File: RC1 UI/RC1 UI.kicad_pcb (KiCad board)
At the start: 2 copper layers, 99.1 x 99.1 mm, 45 parts, among them J1 KB, J2 RC1_UI_Port, M1 Mounting, M2 Mounting, M3 Mounting, M4 Mounting, Q1 2N3906, Q2 2N3906, Q3 2N3906, Q4 2N3906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

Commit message: Added serial to UI schematic
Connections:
- net /ROW_1 renamed /ROW1
- J1 pad 1: /2A6 -> /PA6
- J1 pad 10: /ROW_0 -> /ROW2
- J1 pad 12: (no net) -> /KP_ST
- J1 pad 13: (no net) -> /KP_RS
- J1 pad 15: (no net) -> SST_OUT
- J1 pad 2: /2A5 -> /PA5
- J1 pad 3: /2A4 -> /PA4
- J1 pad 4: /2A3 -> /PA3
- J1 pad 5: /2A2 -> /PA2
- J1 pad 6: /2A1 -> /PA1
- J1 pad 7: /2A0 -> /PA0
- J1 pad 8: /ROW_2 -> /ROW0
- J2 pad 1: (no net) -> GND
- J2 pad 12: (no net) -> /PA0
- J2 pad 13: (no net) -> /PA6
- J2 pad 14: (no net) -> /PA1
- J2 pad 15: (no net) -> /PA5
- J2 pad 16: (no net) -> /PA2
- J2 pad 17: (no net) -> /PA4
- J2 pad 18: (no net) -> /PA3
- J2 pad 2: (no net) -> GND
- J2 pad 3: (no net) -> /PB4
- J2 pad 33: (no net) -> SST_OUT
- J2 pad 34: (no net) -> SYNC
- J2 pad 35: (no net) -> K7
- J2 pad 37: (no net) -> /KP_RS
- J2 pad 38: (no net) -> /KP_ST
- J2 pad 4: (no net) -> /PB3
- J2 pad 6: (no net) -> /PB2
- J2 pad 8: (no net) -> /PB1
- U1 pad 1: /ROW_0 -> /ROW0
- U1 pad 12: (no net) -> /PB4
- U1 pad 13: (no net) -> /PB3
- U1 pad 14: (no net) -> /PB2
- U1 pad 15: (no net) -> /PB1
- U1 pad 3: /ROW_2 -> /ROW2
- U2 pad 1: /2A0 -> /PA0
- U2 pad 11: /2A4 -> /PA4
- U2 pad 13: /2A1 -> /PA0
- U2 pad 3: /2A2 -> /PA2
- U2 pad 5: /2A5 -> /PA5
- U2 pad 9: /2A6 -> /PA6
- U3 pad 1: (no net) -> K7
- U3 pad 2: (no net) -> SYNC
- U3 pad 5: /2A3 -> /PA3

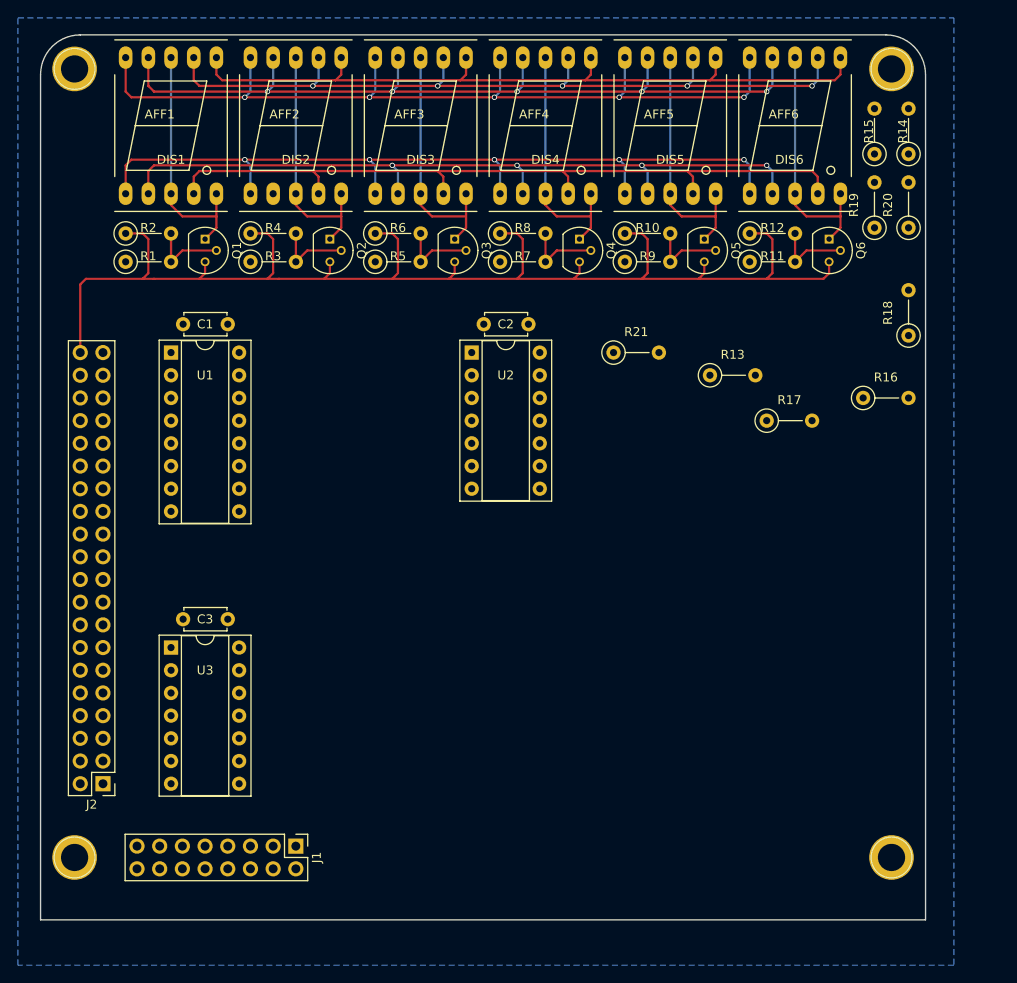
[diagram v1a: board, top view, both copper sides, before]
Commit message: UI layout done
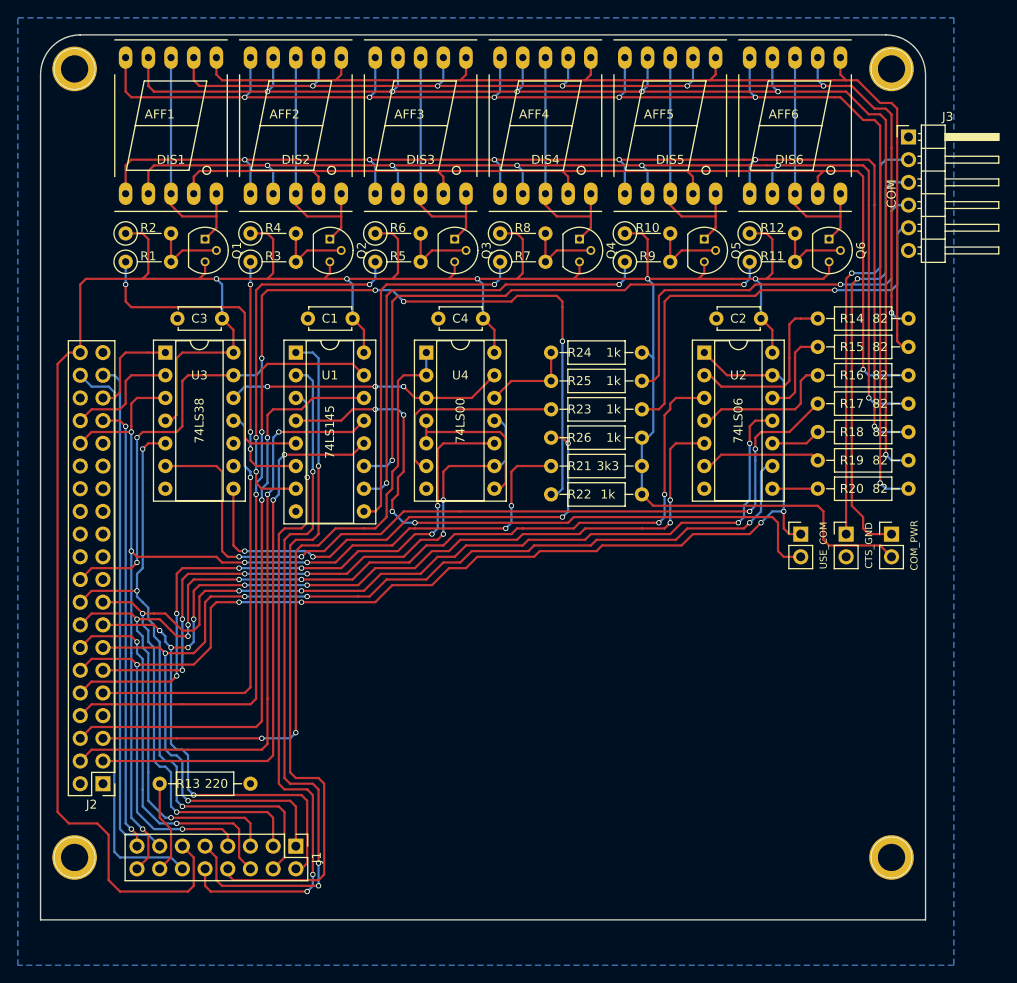
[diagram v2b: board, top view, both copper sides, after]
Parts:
- added C4: 100nF, Capacitors_THT:C_Disc_D4.7mm_W2.5mm_P5.00mm, F.Cu at (157.5, 68.6)
- added J3: COM, Pin_Headers:Pin_Header_Angled_1x06_Pitch2.54mm, F.Cu at (205.1, 48.3)
- added JP1: COM_PWR, Pin_Headers:Pin_Header_Straight_1x02_Pitch2.54mm, F.Cu at (203.2, 92.7)
- added JP2: CTS_GND, Pin_Headers:Pin_Header_Straight_1x02_Pitch2.54mm, F.Cu at (198.1, 92.7)
- added JP3: USE_COM, Pin_Headers:Pin_Header_Straight_1x02_Pitch2.54mm, F.Cu at (193.0, 92.7)
- added R22: 1k, Resistors_THT:R_Axial_DIN0207_L6.3mm_D2.5mm_P10.16mm_Horizontal, F.Cu at (175.3, 88.3)
- added R23: 1k, Resistors_THT:R_Axial_DIN0207_L6.3mm_D2.5mm_P10.16mm_Horizontal, F.Cu at (175.3, 78.7)
- added R24: 1k, Resistors_THT:R_Axial_DIN0207_L6.3mm_D2.5mm_P10.16mm_Horizontal, F.Cu at (175.3, 72.4)
- added R25: 1k, Resistors_THT:R_Axial_DIN0207_L6.3mm_D2.5mm_P10.16mm_Horizontal, F.Cu at (175.3, 75.6)
- added R26: 1k, Resistors_THT:R_Axial_DIN0207_L6.3mm_D2.5mm_P10.16mm_Horizontal, F.Cu at (175.3, 81.9)
- added U4: 74LS00, Housings_DIP:DIP-14_W7.62mm_Socket, F.Cu at (151.1, 72.4)
- R13, R14, R15, R16, R17, R18, R19, R20, R21: footprint Resistors_THT:R_Axial_DIN0207_L6.3mm_D2.5mm_P5.08mm_Vertical -> Resistors_THT:R_Axial_DIN0207_L6.3mm_D2.5mm_P10.16mm_Horizontal
- moved R13 68.8 mm to (131.4, 120.7), turned to 180 degrees
- moved C3 33.7 mm to (128.3, 68.6)
- moved U3 33.0 mm to (121.9, 72.4)
- moved R20 30.9 mm to (194.9, 87.6), turned to 0 degrees
- moved R19 26.8 mm to (194.9, 84.5), turned to 0 degrees
- moved C2 26.0 mm to (188.6, 68.6)
- moved U2 26.0 mm to (182.2, 72.4)
- moved R15 22.5 mm to (194.9, 71.8), turned to 0 degrees
- moved R14 21.0 mm to (194.9, 68.6), turned to 0 degrees
- moved R18 14.8 mm to (194.9, 81.3), turned to 0 degrees
- moved R21 14.5 mm to (165.1, 85.1)
- moved C1 14.0 mm to (142.9, 68.6)
- moved U1 14.0 mm to (136.5, 72.4)
- moved R17 6.02 mm to (194.9, 78.1)
- moved R16 5.68 mm to (194.9, 74.9)
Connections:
- J2 pad 10: (no net) -> /PB0
- J2 pad 11: (no net) -> /PA7
- J2 pad 20: (no net) -> TAPE
- J2 pad 32: (no net) -> SST_IN
- J2 pad 5: (no net) -> /PB5
- J2 pad 9: (no net) -> /PB7
- U1 pad 4: (no net) -> Net-(JP3-Pad2)
- U3 pad 10: (no net) -> GND
- U3 pad 11: (no net) -> /PB7
- U3 pad 12: (no net) -> Net-(U3-Pad12)
- U3 pad 13: (no net) -> TAPE
- U3 pad 8: (no net) -> Net-(R26-Pad2)
- U3 pad 9: (no net) -> GND
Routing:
- net VCC: track 149.1 -> 339.4 mm, vias 0 -> 5
- net /PA0: track 0.00 -> 147.7 mm, vias 0 -> 6
- net /PA4: track 0.00 -> 131.8 mm, vias 0 -> 6
- net /PA2: track 0.00 -> 128.8 mm, vias 0 -> 8
- net /PA5: track 0.00 -> 125.8 mm, vias 0 -> 9
- net /PA6: track 0.00 -> 123.8 mm, vias 0 -> 5
- net SST_IN: track 0.00 -> 119.7 mm, vias 0 -> 7
- net TAPE: track 0.00 -> 106.9 mm, vias 0 -> 6
- net Net-(R17-Pad1): track 0.00 -> 94.0 mm, vias 0 -> 4
- net /ROW1: track 0.00 -> 80.2 mm, vias 0 -> 3
- net /ROW0: track 0.00 -> 78.0 mm, vias 0 -> 1
- net /PB5: track 0.00 -> 75.7 mm, vias 0 -> 2
- net /ROW2: track 0.00 -> 75.5 mm, vias 0 -> 3
- net Net-(JP3-Pad2): track 0.00 -> 74.4 mm, vias 0 -> 4
- net /PA3: track 0.00 -> 71.0 mm, vias 0 -> 3
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
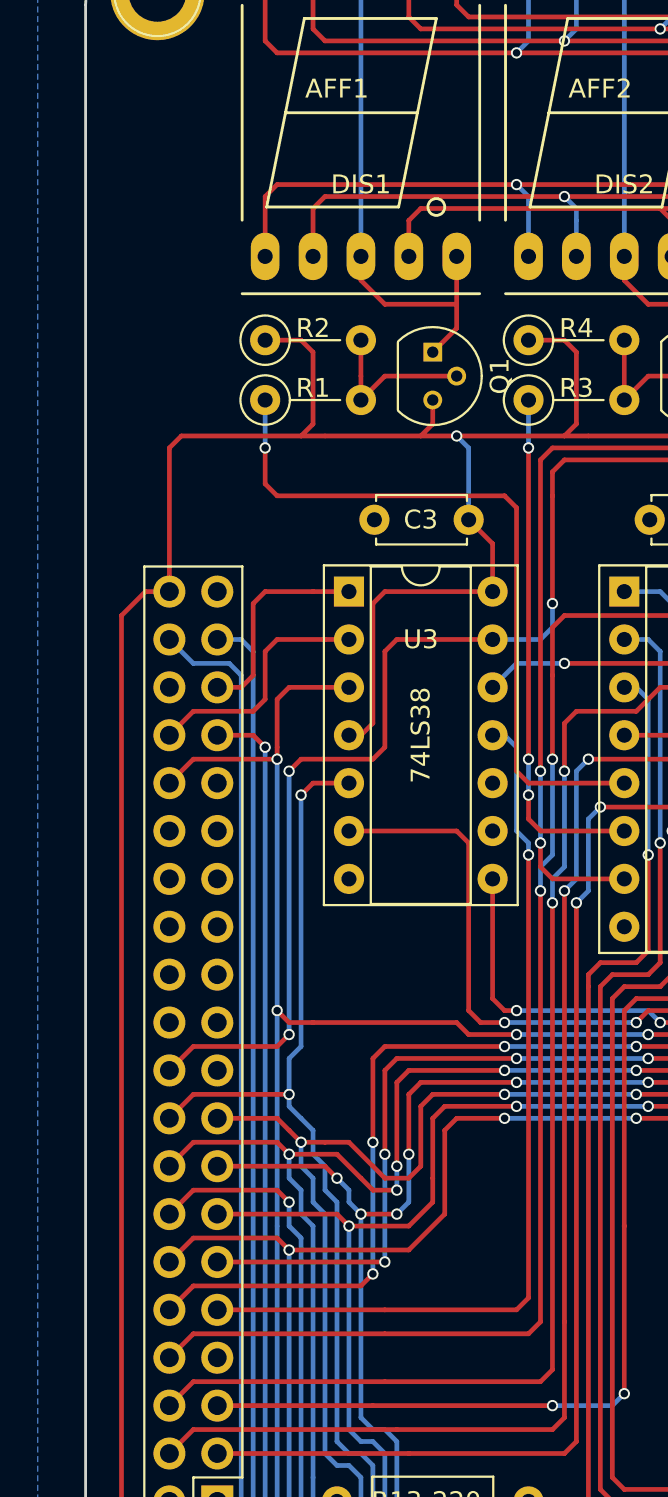
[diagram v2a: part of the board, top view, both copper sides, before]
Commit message: Added silkscreen title
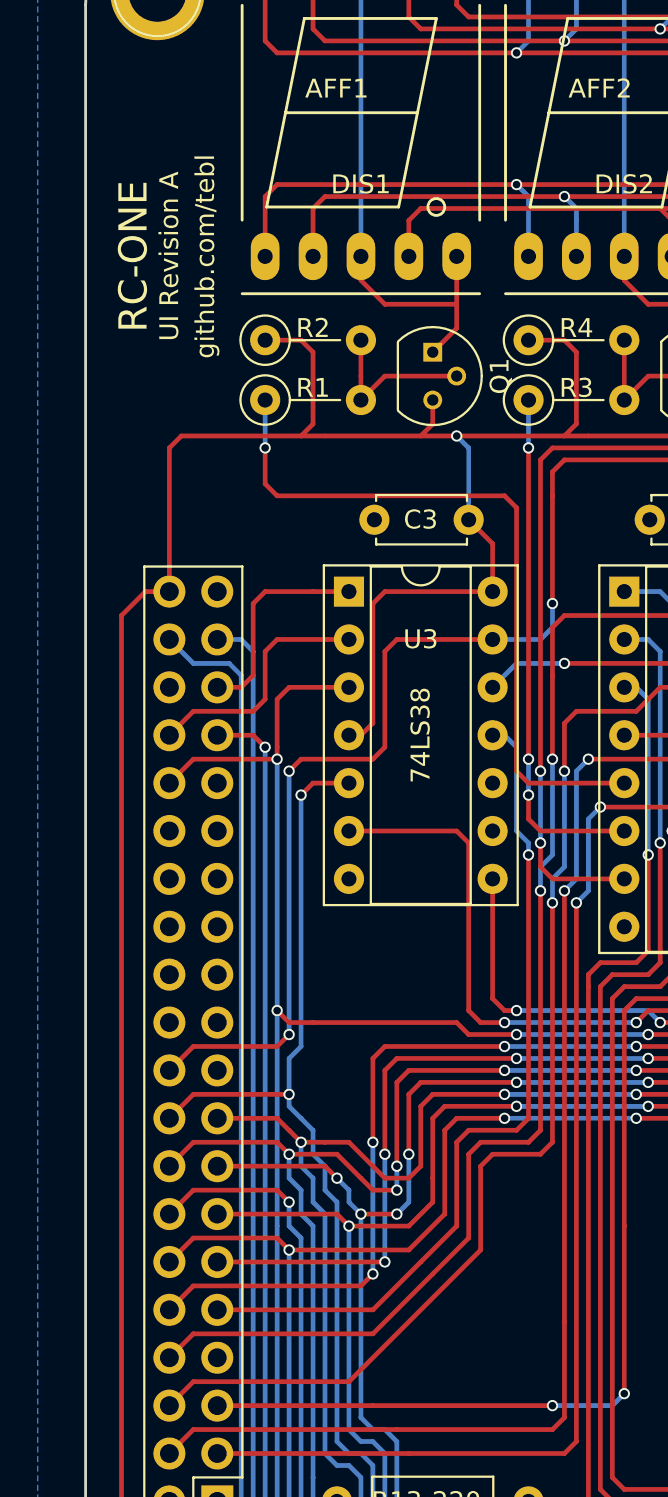
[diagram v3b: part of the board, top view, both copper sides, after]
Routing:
- net /PB2: track 67.2 -> 62.8 mm
- net /PB1: track 69.8 -> 66.4 mm
- net /PB7: track 47.8 -> 44.8 mm
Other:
- board text added: "RC-ONE"
- board text added: "UI Revision A"
- board text added: "github.com/tebl"
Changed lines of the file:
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@@
     (area 107.874999 36.754999 207.085001 135.965001)
     (thickness 1.6)
-    (drawings 6)
-    (tracks 1226)
+    (drawings 9)
+    (tracks 1239)
     (zones 0)
     (modules 56)
@@
     )
   )
+  (gr_text "UI Revision A" (at 112.395 54.61 90) (layer F.SilkS)
+    (effects (font (size 1 1) (thickness 0.15)))
+  )
+  (gr_text github.com/tebl (at 114.3 54.61 90) (layer F.SilkS)
+    (effects (font (size 1 1) (thickness 0.15)))
+  )
+  (gr_text RC-ONE (at 110.49 54.61 90) (layer F.SilkS)
+    (effects (font (size 1.5 1.5) (thickness 0.3)))
+  )
   (gr_line (start 207.01 41.275) (end 207.01 135.89) (angle 90) (layer Edge.Cuts) (width 0.15))
   (gr_line (start 107.95 41.275) (end 107.95 135.89) (angle 90) (layer Edge.Cuts) (width 0.15))
@@
   (via (at 134.62 81.28) (size 0.6) (drill 0.4) (layers F.Cu B.Cu) (net 51))
   (segment (start 142.875 81.28) (end 134.62 81.28) (width 0.25) (layer F.Cu) (net 51))
+  (segment (start 132.715 101.6) (end 132.08 102.235) (width 0.25) (layer F.Cu) (net 52))
+  (segment (start 128.905 107.315) (end 121.92 114.3) (width 0.25) (layer F.Cu) (net 52))
+  (segment (start 128.905 102.87) (end 128.905 107.315) (width 0.25) (layer F.Cu) (net 52))
+  (segment (start 129.54 102.235) (end 128.905 102.87) (width 0.25) (layer F.Cu) (net 52))
+  (segment (start 132.08 102.235) (end 129.54 102.235) (width 0.25) (layer F.Cu) (net 52))
   (segment (start 144.145 77.47) (end 138.43 77.47) (width 0.25) (layer F.Cu) (net 52))
   (segment (start 138.43 77.47) (end 137.16 78.74) (width 0.25) (layer F.Cu) (net 52))
   (segment (start 133.35 81.915) (end 133.35 86.995) (width 0.25) (layer B.Cu) (net 52))
-  (segment (start 113.665 114.3) (end 123.825 114.3) (width 0.25) (layer F.Cu) (net 52))
+  (segment (start 113.665 114.3) (end 121.92 114.3) (width 0.25) (layer F.Cu) (net 52))
   (segment (start 112.395 115.57) (end 113.665 114.3) (width 0.25) (layer F.Cu) (net 52))
   (segment (start 137.16 78.74) (end 133.985 78.74) (width 0.25) (layer F.Cu) (net 52))
@@
   (segment (start 133.35 79.375) (end 133.35 81.915) (width 0.25) (layer F.Cu) (net 52))
   (via (at 133.35 81.915) (size 0.6) (drill 0.4) (layers F.Cu B.Cu) (net 52))
-  (segment (start 132.08 114.3) (end 123.825 114.3) (width 0.25) (layer F.Cu) (net 52))
-  (segment (start 132.715 113.665) (end 132.08 114.3) (width 0.25) (layer F.Cu) (net 52))
-  (segment (start 132.715 88.9) (end 132.715 113.665) (width 0.25) (layer F.Cu) (net 52))
+  (segment (start 132.715 88.9) (end 132.715 101.6) (width 0.25) (layer F.Cu) (net 52))
   (via (at 132.715 88.9) (size 0.6) (drill 0.4) (layers F.Cu B.Cu) (net 52))
   (segment (start 132.715 87.63) (end 132.715 88.9) (width 0.25) (layer B.Cu) (net 52))
   (segment (start 133.35 86.995) (end 132.715 87.63) (width 0.25) (layer B.Cu) (net 52))
+  (segment (start 126.365 108.585) (end 123.19 111.76) (width 0.25) (layer F.Cu) (net 53))
+  (segment (start 123.19 111.76) (end 122.555 111.76) (width 0.25) (layer F.Cu) (net 53))
+  (segment (start 132.08 100.965) (end 131.445 101.6) (width 0.25) (layer F.Cu) (net 53))
+  (segment (start 128.27 106.68) (end 126.365 108.585) (width 0.25) (layer F.Cu) (net 53))
+  (segment (start 128.27 102.235) (end 128.27 106.68) (width 0.25) (layer F.Cu) (net 53))
+  (segment (start 128.905 101.6) (end 128.27 102.235) (width 0.25) (layer F.Cu) (net 53))
+  (segment (start 131.445 101.6) (end 128.905 101.6) (width 0.25) (layer F.Cu) (net 53))
   (segment (start 132.715 76.835) (end 132.715 74.295) (width 0.25) (layer F.Cu) (net 53))
   (segment (start 142.875 73.66) (end 144.145 74.93) (width 0.25) (layer F.Cu) (net 53))
@@
   (segment (start 132.715 74.295) (end 133.35 73.66) (width 0.25) (layer F.Cu) (net 53))
   (segment (start 132.715 86.36) (end 132.08 86.995) (width 0.25) (layer B.Cu) (net 53))
-  (segment (start 132.08 111.125) (end 131.445 111.76) (width 0.25) (layer F.Cu) (net 53))
-  (segment (start 132.08 88.265) (end 132.08 111.125) (width 0.25) (layer F.Cu) (net 53))
+  (segment (start 132.08 88.265) (end 132.08 100.965) (width 0.25) (layer F.Cu) (net 53))
   (via (at 132.08 88.265) (size 0.6) (drill 0.4) (layers F.Cu B.Cu) (net 53))
   (segment (start 132.08 86.995) (end 132.08 88.265) (width 0.25) (layer B.Cu) (net 53))
-  (segment (start 113.665 111.76) (end 123.825 111.76) (width 0.25) (layer F.Cu) (net 53))
+  (segment (start 113.665 111.76) (end 122.555 111.76) (width 0.25) (layer F.Cu) (net 53))
   (segment (start 113.665 111.76) (end 112.395 113.03) (width 0.25) (layer F.Cu) (net 53))
-  (segment (start 131.445 111.76) (end 123.825 111.76) (width 0.25) (layer F.Cu) (net 53))
   (segment (start 132.715 81.28) (end 132.715 86.36) (width 0.25) (layer B.Cu) (net 53))
   (via (at 132.715 81.28) (size 0.6) (drill 0.4) (layers F.Cu B.Cu) (net 53))
@@
   (segment (start 148.59 74.93) (end 147.955 75.565) (width 0.25) (layer F.Cu) (net 56))
   (segment (start 151.13 74.93) (end 151.13 72.39) (width 0.25) (layer B.Cu) (net 56))
+  (segment (start 125.73 107.95) (end 123.19 110.49) (width 0.25) (layer F.Cu) (net 57))
+  (segment (start 123.19 110.49) (end 122.555 110.49) (width 0.25) (layer F.Cu) (net 57))
+  (segment (start 131.445 100.33) (end 130.81 100.965) (width 0.25) (layer F.Cu) (net 57))
+  (segment (start 127.635 106.045) (end 125.73 107.95) (width 0.25) (layer F.Cu) (net 57))
+  (segment (start 127.635 101.6) (end 127.635 106.045) (width 0.25) (layer F.Cu) (net 57))
+  (segment (start 128.27 100.965) (end 127.635 101.6) (width 0.25) (layer F.Cu) (net 57))
+  (segment (start 130.81 100.965) (end 128.27 100.965) (width 0.25) (layer F.Cu) (net 57))
   (segment (start 129.54 80.01) (end 130.175 80.01) (width 0.25) (layer B.Cu) (net 57))
   (segment (start 130.175 80.01) (end 130.81 80.645) (width 0.25) (layer B.Cu) (net 57))
@@
   (segment (start 131.445 85.725) (end 131.445 86.36) (width 0.25) (layer B.Cu) (net 57))
   (via (at 131.445 86.36) (size 0.6) (drill 0.4) (layers F.Cu B.Cu) (net 57))
-  (segment (start 131.445 86.36) (end 131.445 109.855) (width 0.25) (layer F.Cu) (net 57))
-  (segment (start 131.445 109.855) (end 130.81 110.49) (width 0.25) (layer F.Cu) (net 57))
-  (segment (start 130.81 110.49) (end 123.825 110.49) (width 0.25) (layer F.Cu) (net 57))
-  (segment (start 114.935 110.49) (end 123.825 110.49) (width 0.25) (layer F.Cu) (net 57))
+  (segment (start 131.445 86.36) (end 131.445 100.33) (width 0.25) (layer F.Cu) (net 57))
+  (segment (start 114.935 110.49) (end 122.555 110.49) (width 0.25) (layer F.Cu) (net 57))
   (via (at 123.19 108.585) (size 0.6) (drill 0.4) (layers F.Cu B.Cu) (net 58))
   (segment (start 123.19 108.585) (end 122.555 109.22) (width 0.25) (layer F.Cu) (net 58))
